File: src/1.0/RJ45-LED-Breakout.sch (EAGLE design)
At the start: 5 parts, among them J1 RJ45-RJHSE-5481, J2 M06SQ1, J3 M06SQ1

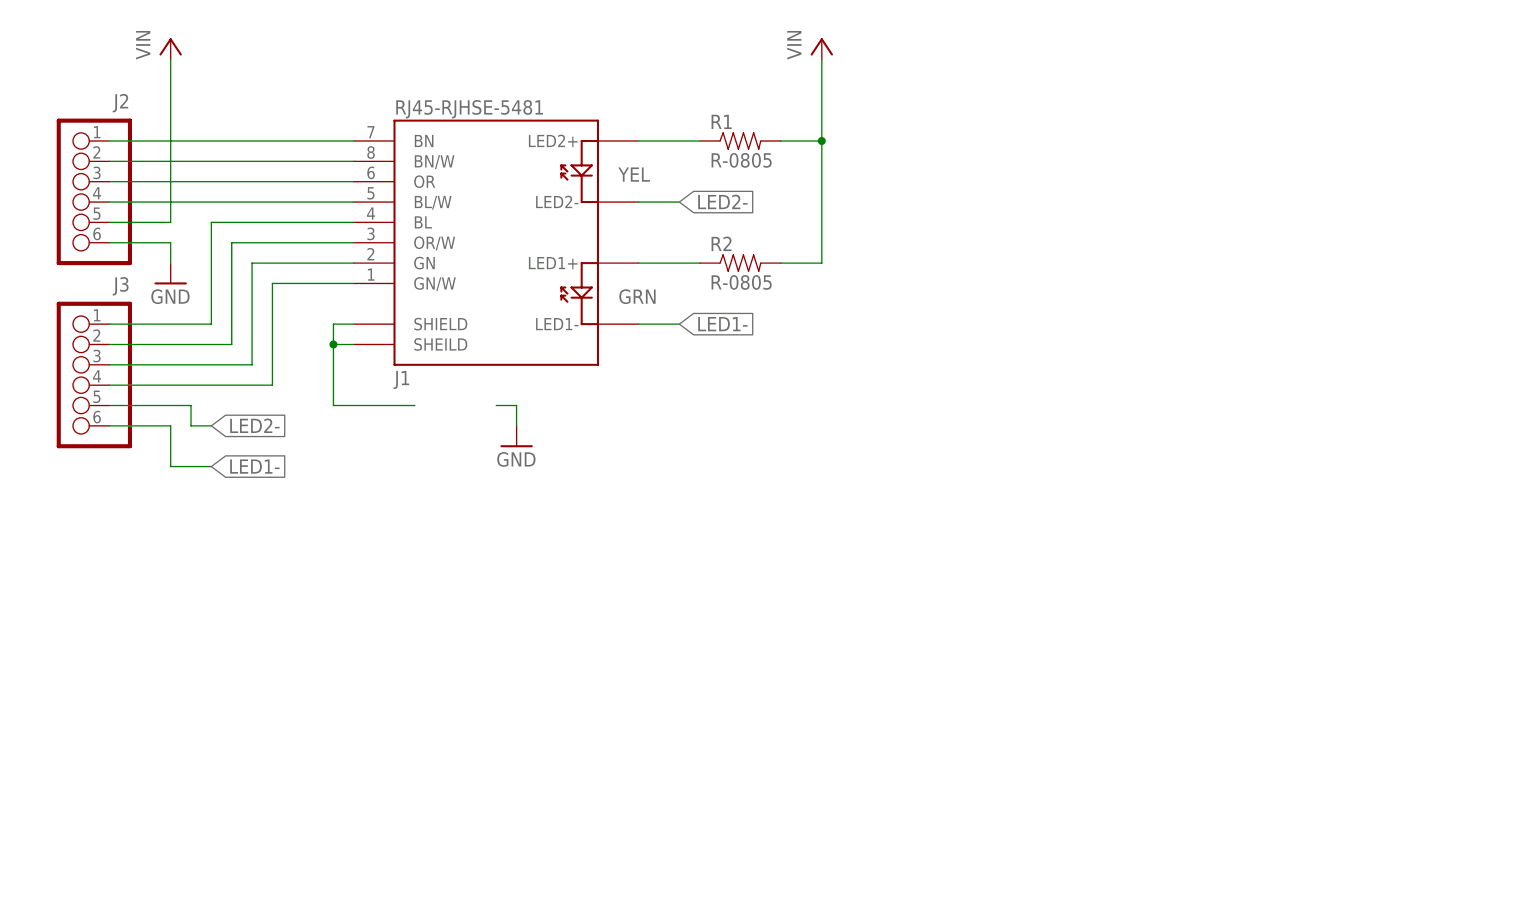
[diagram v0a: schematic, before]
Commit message: Board mostly laid out but pins 7/8 are switched. Fix that then reroute and it is basicaly done. Need to add some more info on silk.
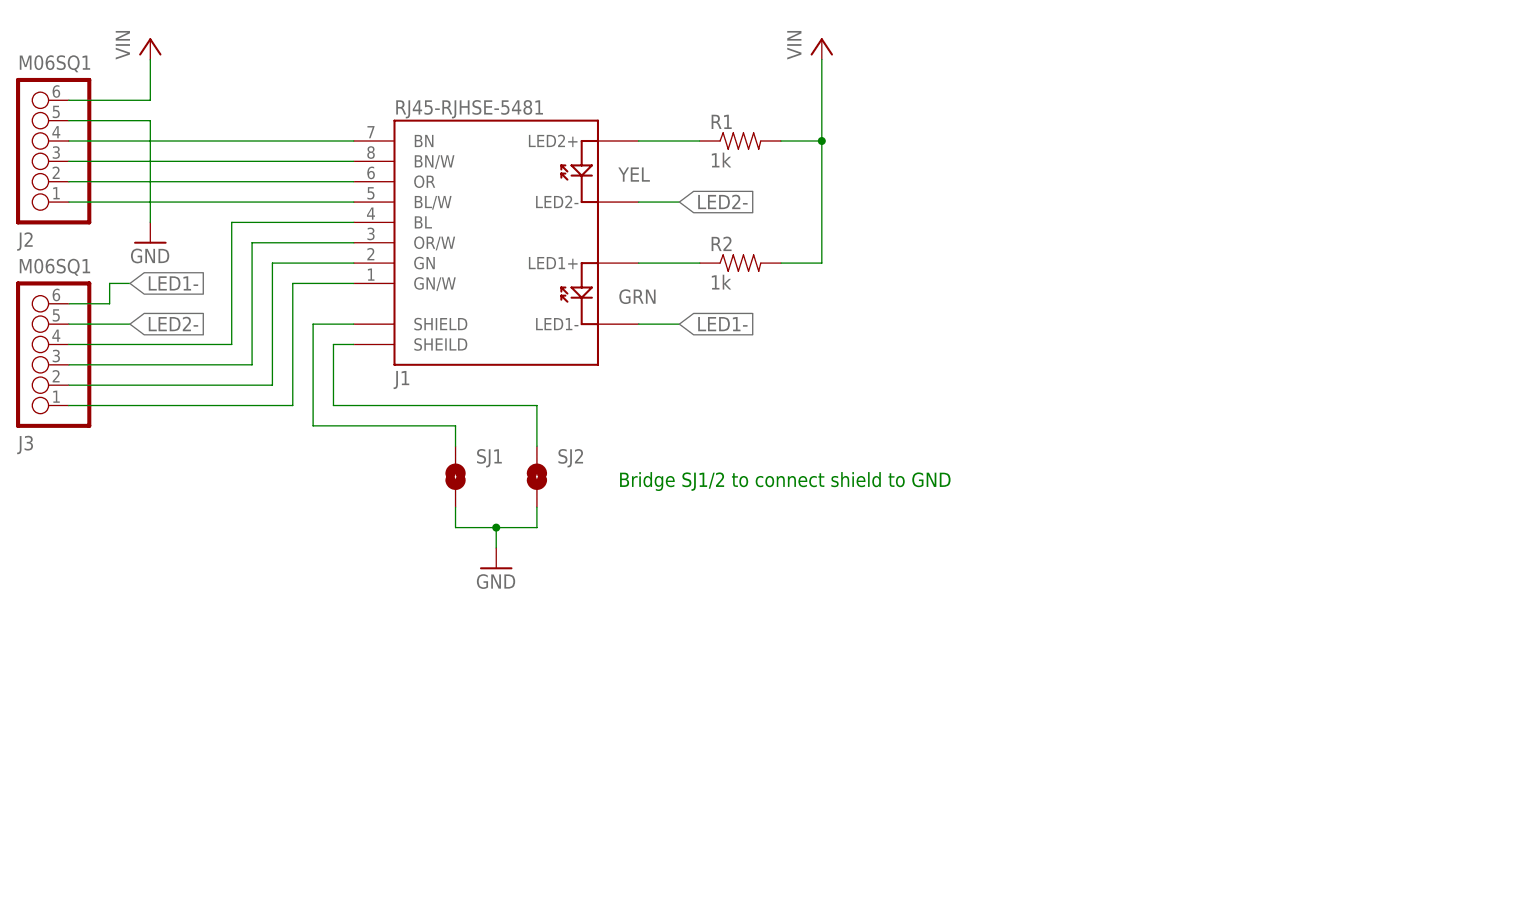
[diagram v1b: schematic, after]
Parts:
- added SJ1, SJ2: SJ_1WAY, LoganSmith-Connectors:SJ_1WAY
- R1, R2: value R-0805 -> 1k; device LoganSmith-Resistors:R-0805 -> LoganSmith-Resistors:1K-5%-0805
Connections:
- net N$10 renamed LED1+
- net N$9 renamed LED2+
- new net N$12: J1.SHEILD@1, SJ2.1
- net GND: now also J2.5, SJ1.2, SJ2.2; no longer J2.6
- net N$1: now also J1.BL/W; no longer J1.BN
- net N$11: now also SJ1.1; no longer J1.SHEILD@1
- net N$2: now also J1.OR; no longer J1.BN/W
- net N$3: now also J1.BN/W; no longer J1.OR
- net N$4: now also J1.BN; no longer J1.BL/W
- net N$5: now also J3.4; no longer J3.1
- net N$6: now also J3.3; no longer J3.2
- net N$7: now also J3.2; no longer J3.3
- net N$8: now also J3.1; no longer J3.4
- net VIN: now also J2.6; no longer J2.5
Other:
- note added: "Bridge SJ1/2 to connect shield to GND"
- moved on the sheet: J2, J3

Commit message: Almost ready for release. Need to create BOM and review all connections. Also look over schematic and possibly clean things up if necessary.
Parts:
- added LOGO1: OSHW-LOGOM, SparkFun-Aesthetics:OSHW-LOGOM
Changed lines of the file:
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@@
 <?xml version="1.0" encoding="utf-8"?>
 <!DOCTYPE eagle SYSTEM "eagle.dtd">
-<eagle version="6.6.0">
+<eagle version="6.3">
 <drawing>
 <settings>
@@
 <part name="J2" library="LoganSmith-Connectors" deviceset="M06?" device="SQ1"/>
 <part name="J3" library="LoganSmith-Connectors" deviceset="M06?" device="SQ1"/>
+<part name="LOGO1" library="SparkFun-Aesthetics" deviceset="OSHW-LOGO" device="M"/>
 </parts>
 <sheets>
@@
 <instance part="J2" gate="G$1" x="-12.7" y="38.1"/>
 <instance part="J3" gate="G$1" x="-12.7" y="12.7"/>
+<instance part="LOGO1" gate="G$1" x="162.56" y="-38.1"/>
 </instances>
 <busses>

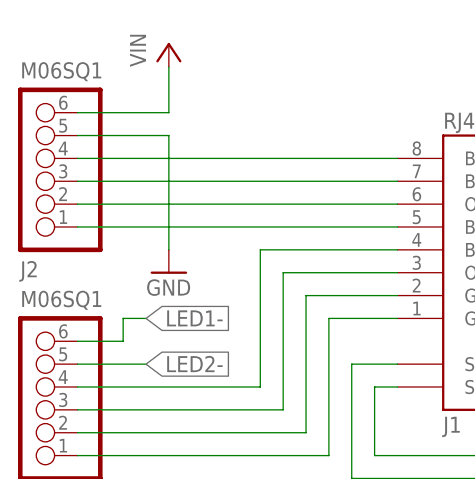
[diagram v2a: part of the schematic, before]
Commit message: Board has been ordered. Updated README, finalized board layout and silk. Need to create BOM and release 1.0.
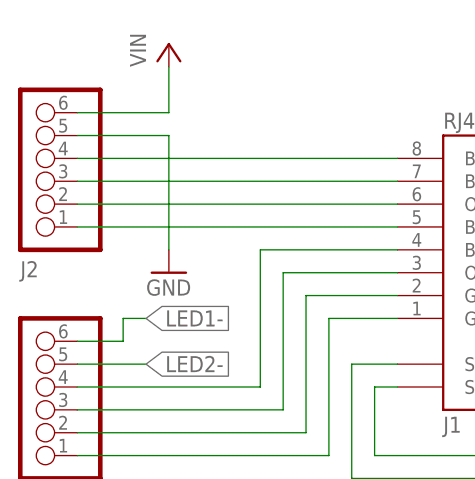
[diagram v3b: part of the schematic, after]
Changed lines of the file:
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@@
 <part name="SJ2" library="LoganSmith-Connectors" deviceset="SJ_1WAY" device="" value=""/>
 <part name="FRAME1" library="SparkFun-Aesthetics" deviceset="FRAME-A4L" device=""/>
-<part name="J2" library="LoganSmith-Connectors" deviceset="M06?" device="SQ1"/>
-<part name="J3" library="LoganSmith-Connectors" deviceset="M06?" device="SQ1"/>
+<part name="J2" library="LoganSmith-Connectors" deviceset="M06?" device="SQ1" value=""/>
+<part name="J3" library="LoganSmith-Connectors" deviceset="M06?" device="SQ1" value=""/>
 <part name="LOGO1" library="SparkFun-Aesthetics" deviceset="OSHW-LOGO" device="M"/>
 </parts>
